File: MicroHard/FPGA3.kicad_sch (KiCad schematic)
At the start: 0 parts

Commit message: fpg
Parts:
- added U4: XC7A100T-FTG256, symbol FPGA_Xilinx_Artix7:XC7A100T-FTG256

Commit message: extra files
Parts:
- added C44: 47u, symbol Device:C
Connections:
- net +3.3V: now reaches U4.L6 (VCCO_0)
- net +3.3V: now also C44.1
- new net GND: C44.2
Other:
- moved on the sheet: U4C
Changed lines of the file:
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@@
 	(generator_version "8.0")
 	(paper "A4")
+	(wire
+		(pts
+			(xy 26.67 158.75) (xy 26.67 161.29)
+		)
+		(stroke
+			(width 0)
+			(type default)
+		)
+	)
+	(wire
+		(pts
+			(xy 26.67 168.91) (xy 26.67 170.18)
+		)
+		(stroke
+			(width 0)
+			(type default)
+		)
+	)
+	(wire
+		(pts
+			(xy 99.06 49.53) (xy 99.06 55.88)
+		)
+		(stroke
+			(width 0)
+			(type default)
+		)
+	)
+	(global_label "+3.3V"
+		(shape input)
+		(at 26.67 158.75 90)
+		(fields_autoplaced yes)
+		(effects
+			(font
+				(size 1.27 1.27)
+			)
+			(justify left)
+		)
+		(property "Intersheetrefs" "${INTERSHEET_REFS}"
+			(at 26.67 150.08 90)
+			(effects
+				(font
+					(size 1.27 1.27)
+				)
+				(justify left)
+				(hide yes)
+			)
+		)
+	)
+	(global_label "+3.3V"
+		(shape input)
+		(at 99.06 49.53 90)
+		(fields_autoplaced yes)
+		(effects
+			(font
+				(size 1.27 1.27)
+			)
+			(justify left)
+		)
+		(property "Intersheetrefs" "${INTERSHEET_REFS}"
+			(at 99.06 40.86 90)
+			(effects
+				(font
+					(size 1.27 1.27)
+				)
+				(justify left)
+				(hide yes)
+			)
+		)
+	)
+	(symbol
+		(lib_id "power:GND")
+		(at 26.67 170.18 0)
+		(unit 1)
+		(exclude_from_sim no)
+		(in_bom yes)
+		(on_board yes)
+		(dnp no)
+		(fields_autoplaced yes)
+		(property "Reference" "#PWR013"
+			(at 26.67 176.53 0)
+			(effects
+				(font
+					(size 1.27 1.27)
+				)
+				(hide yes)
+			)
+		)
+		(property "Value" "GND"
+			(at 26.67 175.26 0)
+			(effects
+				(font
+					(size 1.27 1.27)
+				)
+			)
+		)
+		(property "Footprint" ""
+			(at 26.67 170.18 0)
+			(effects
+				(font
+					(size 1.27 1.27)
+				)
+				(hide yes)
+			)
+		)
+		(property "Datasheet" ""
+			(at 26.67 170.18 0)
+			(effects
+				(font
+					(size 1.27 1.27)
+				)
+				(hide yes)
+			)
+		)
+		(property "Description" "Power symbol creates a global label with name \"GND\" , ground"
+			(at 26.67 170.18 0)
+			(effects
+				(font
+					(size 1.27 1.27)
+				)
+				(hide yes)
+			)
+		)
+		(pin "1"
+		)
+		(instances
+			(project ""
+				(path "/578bd531-a491-4b15-a479-460d159ffc14/e381883e-e672-4900-88a5-08b94f970a88/5897012d-c01f-459a-b65a-eba111a7dafb"
+					(reference "#PWR013")
+					(unit 1)
+				)
+			)
+		)
+	)
 	(symbol
 		(lib_id "FPGA_Xilinx_Artix7:XC7A100T-FTG256")
-		(at 90.17 88.9 0)
+		(at 71.12 96.52 0)
 		(unit 3)
 		(exclude_from_sim no)
@@
 		(fields_autoplaced yes)
 		(property "Reference" "U4"
-			(at 57.15 90.8049 0)
+			(at 38.1 98.4249 0)
 			(effects
 				(font
@@
 		)
 		(property "Value" "XC7A100T-FTG256"
-			(at 57.15 93.3449 0)
+			(at 38.1 100.9649 0)
 			(effects
 				(font
@@
 		)
 		(property "Footprint" ""
-			(at 90.17 88.9 0)
+			(at 71.12 96.52 0)
 			(effects
 				(font
@@
 		)
 		(property "Datasheet" ""
-			(at 90.17 88.9 0)
+			(at 71.12 96.52 0)
 			(effects
 				(font
@@
 		)
 		(property "Description" "Artix 7 T 100 XC7A100T-FTG256"
-			(at 90.17 88.9 0)
+			(at 71.12 96.52 0)
 			(effects
 				(font
@@
 				)
 			)
+		)
+	)
+	(symbol
+		(lib_id "Device:C")
+		(at 26.67 165.1 0)
+		(unit 1)
+		(exclude_from_sim no)
+		(in_bom yes)
+		(on_board yes)
+		(dnp no)
+		(fields_autoplaced yes)
+		(property "Reference" "C44"
+			(at 30.48 163.8299 0)
+			(effects
+				(font
+					(size 1.27 1.27)
+				)
+				(justify left)
+			)
+		)
+		(property "Value" "47u"
+			(at 30.48 166.3699 0)
+			(effects
+				(font
+					(size 1.27 1.27)
+				)
+				(justify left)
+			)
+		)
+		(property "Footprint" ""
+			(at 27.6352 168.91 0)
+			(effects
+				(font
+					(size 1.27 1.27)
+				)
+				(hide yes)
+			)
+		)
+		(property "Datasheet" "~"
+			(at 26.67 165.1 0)
+			(effects
+				(font
+					(size 1.27 1.27)
+				)
+				(hide yes)
+			)
+		)
+		(property "Description" "Unpolarized capacitor"
+			(at 26.67 165.1 0)
+			(effects
+				(font
+					(size 1.27 1.27)
+				)
+				(hide yes)
+			)
+		)
+		(pin "1"
+		)
+		(pin "2"
+		)
+		(instances
+			(project ""
+				(path "/578bd531-a491-4b15-a479-460d159ffc14/e381883e-e672-4900-88a5-08b94f970a88/5897012d-c01f-459a-b65a-eba111a7dafb"
+					(reference "C44")
+					(unit 1)
+				)
+			)

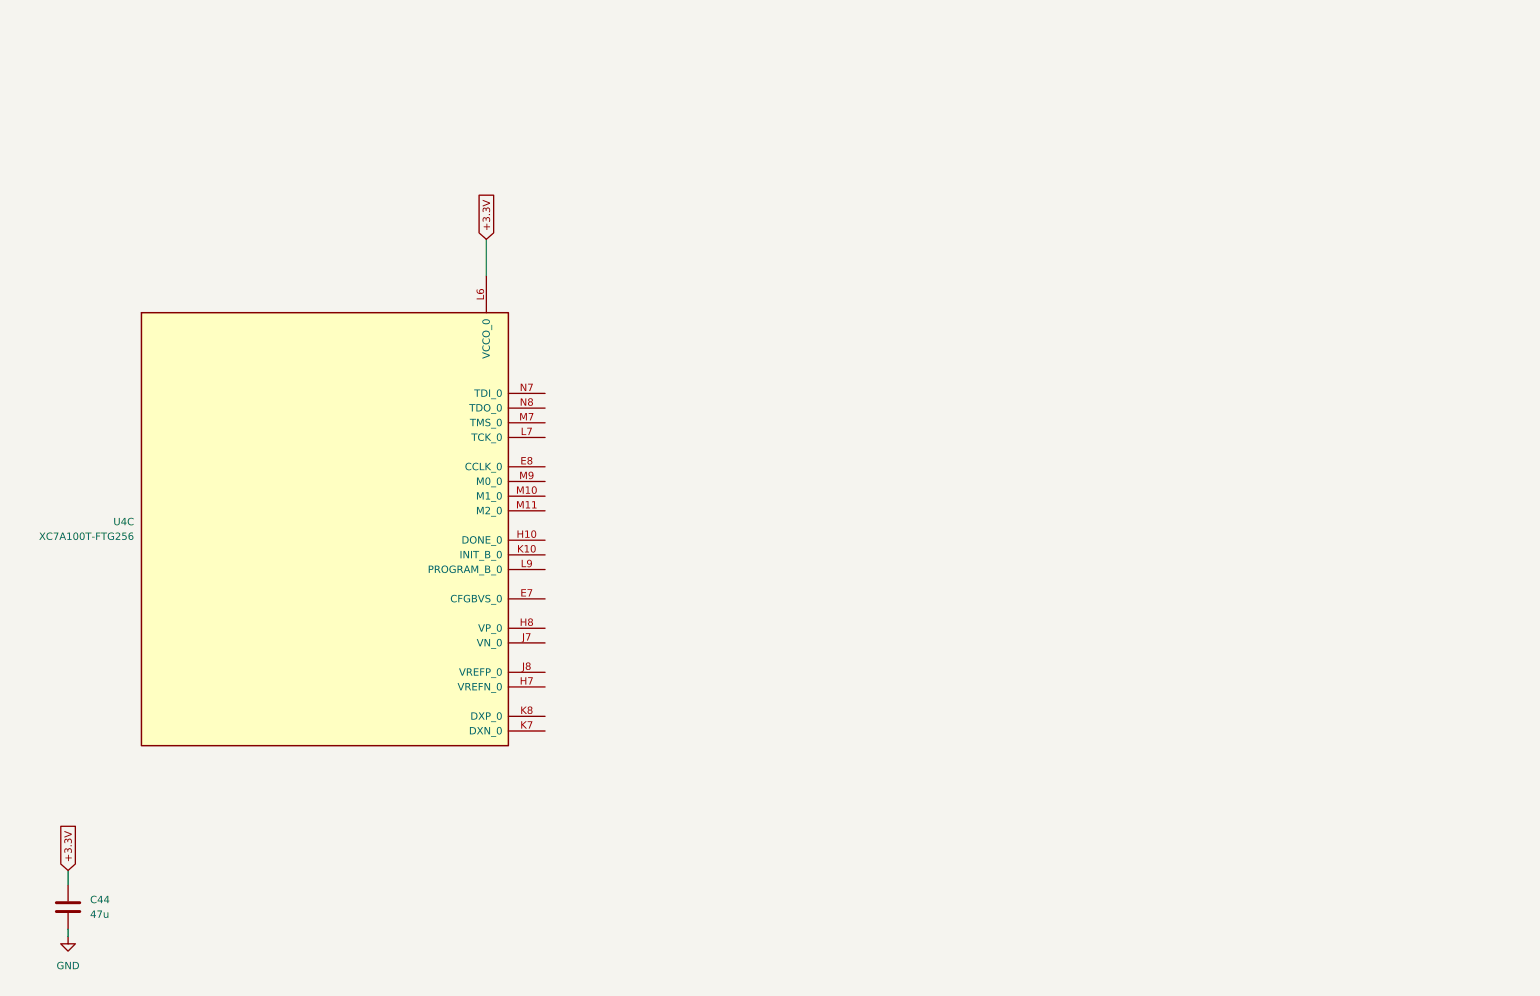
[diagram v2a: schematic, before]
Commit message: feat: finished FPGA config
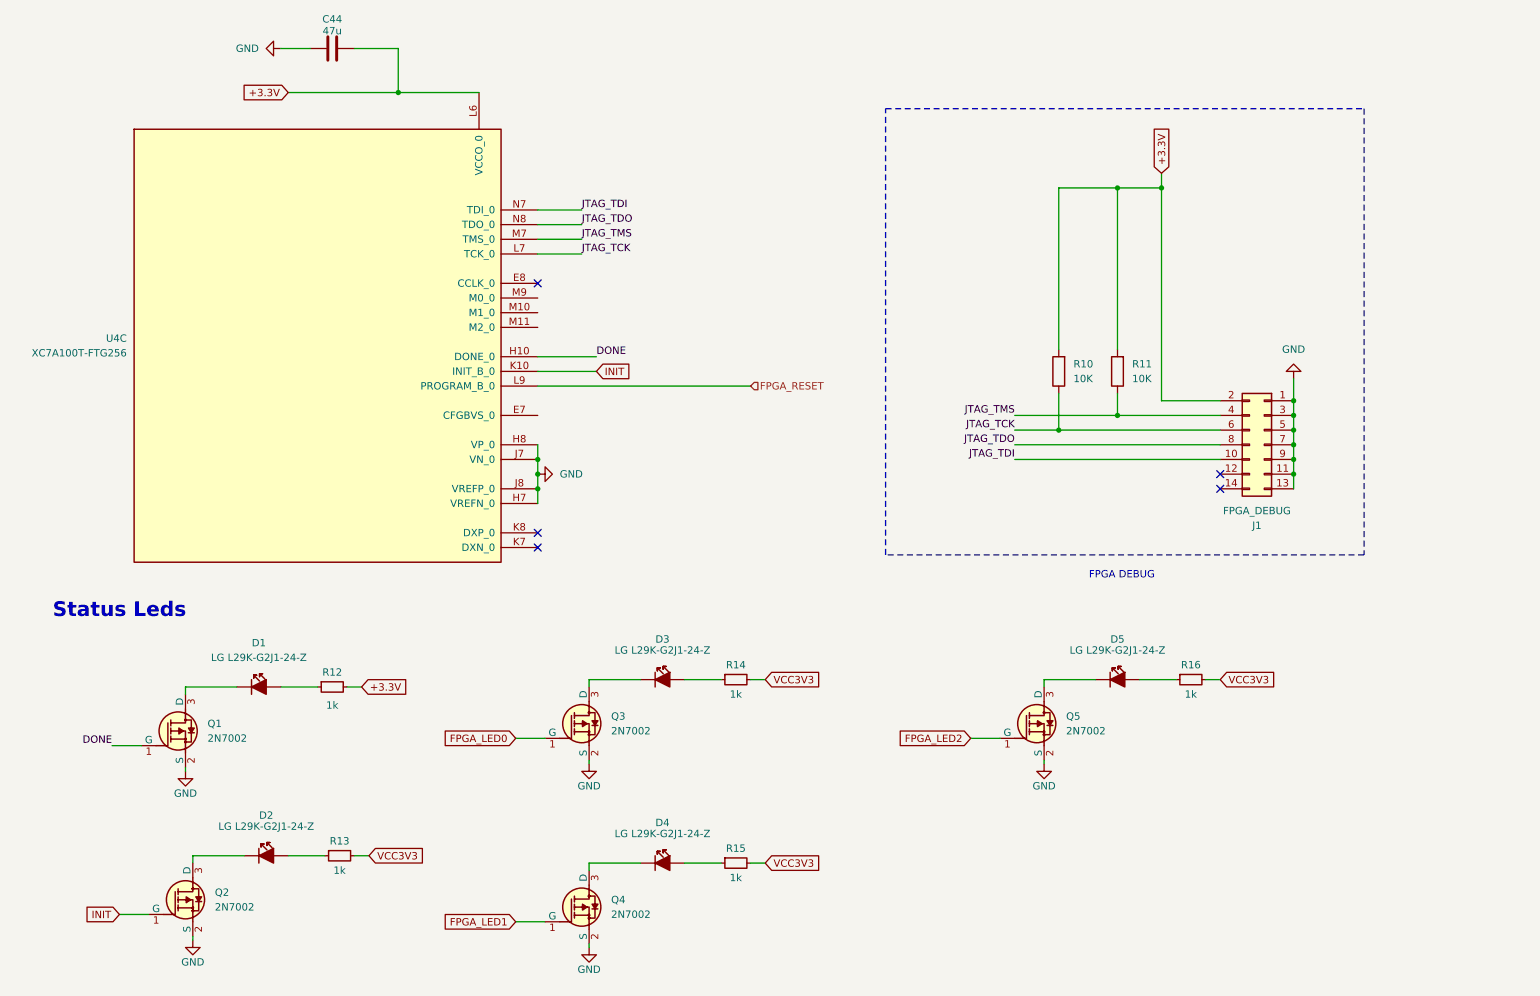
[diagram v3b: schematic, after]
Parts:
- added D1, D2, D3, D4, D5: LED_G_0603_LG_L29K-G2J1-24-Z, antmicro-footprints:LED_0603_1608Metric_G, symbol antmicroLEDIndicationDiscrete:LED_G_0603_LG_L29K-G2J1-24-Z
- added J1: FPGA_DEBUG, symbol Connector_Generic:Conn_02x07_Odd_Even
- added Q1, Q2, Q3, Q4, Q5: 2N7002_SOT-23-3, antmicro-footprints:SOT-23-3, symbol antmicroTransistorsFETsMOSFETsSingle:2N7002_SOT-23-3
- added R10, R11: 10K, symbol Device:R
- added R12, R13, R14, R15, R16: R_1k_0402, antmicro-footprints:R_0402_1005Metric, symbol antmicroResistors0402:R_1k_0402
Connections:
- net +3.3V: now also J1.2 (Pin_2), R10.2, R11.2, R12.2
- net GND: now also U4.H7 (VREFN_0), U4.H8 (VP_0), U4.J7 (VN_0), U4.J8 (VREFP_0), J1.1 (Pin_1), J1.11 (Pin_11), J1.13 (Pin_13), J1.3 (Pin_3), J1.5 (Pin_5), J1.7 (Pin_7), J1.9 (Pin_9), Q1.2 (S), Q2.2 (S), Q3.2 (S), Q4.2 (S), Q5.2 (S)
- net DONE: now reaches U4.H10 (DONE_0)
- net DONE: now also Q1.1 (G)
- net INIT: now reaches U4.K10 (INIT_B_0)
- net INIT: now also Q2.1 (G)
- net JTAG_TCK: now reaches U4.L7 (TCK_0)
- net JTAG_TCK: now also J1.6 (Pin_6), R10.1
- net FPGA_RESET: now reaches U4.L9 (PROGRAM_B_0)
- net JTAG_TMS: now reaches U4.M7 (TMS_0)
- net JTAG_TMS: now also J1.4 (Pin_4), R11.1
- net JTAG_TDI: now reaches U4.N7 (TDI_0)
- net JTAG_TDI: now also J1.10 (Pin_10)
- net JTAG_TDO: now reaches U4.N8 (TDO_0)
- net JTAG_TDO: now also J1.8 (Pin_8)
- new net: D1.1, R12.1
- new net: D5.1, R16.1
- new net: D5.2, Q5.3 (D)
- new net: D3.2, Q3.3 (D)
- new net: D3.1, R14.1
- new net: D2.1, R13.1
- new net: D1.2, Q1.3 (D)
- new net: D4.1, R15.1
- new net: D4.2, Q4.3 (D)
- new net: D2.2, Q2.3 (D)
- new net FPGA_LED0: Q3.1 (G)
- new net FPGA_LED1: Q4.1 (G)
- new net FPGA_LED2: Q5.1 (G)
- new net VCC3V3: R13.2, R14.2, R15.2, R16.2
- no-connect marks 0 -> 5
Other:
- note added: "FPGA DEBUG"
- note added: "Status Leds"
- moved on the sheet: U4C

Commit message: feat: finished Flash mem and FPGA Config
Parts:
- added R17, R19: 4.7k, symbol Device:R
- added R18: 330, symbol Device:R
- added TP1, TP2, TP3: TestPoint, symbol Connector:TestPoint
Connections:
- net +3.3V: now also U4.E7 (CFGBVS_0), U4.M9 (M0_0), R17.1, R18.2, R19.1
- net FPGA_RESET: now also Q1.1 (G), R19.2, TP1.1, TP2.1
- net GND: now also U4.M10 (M1_0), U4.M11 (M2_0)
- net INIT: now also R17.2, TP3.1
- net FPGA_CONFIG_CLOCK: now reaches U4.E8 (CCLK_0)
- net DONE: no longer names the net of U4.H10 (DONE_0)
- net DONE: now also R18.1; no longer Q1.1 (G)
- no-connect marks 5 -> 4
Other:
- note added: "Are these pull ups neccessary"
- moved on the sheet: J1, R10, R11

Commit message: chore
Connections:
- net VCC3V3 is gone; now on net +3.3V: R13.2, R14.2, R15.2, R16.2
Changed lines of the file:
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@@
+		)
+	)
+	(global_label "+3.3V"
+		(shape input)
+		(at 147.32 125.73 0)
+		(fields_autoplaced yes)
+		(effects
+			(font
+				(size 1.27 1.27)
+			)
+			(justify left)
+		)
+		(property "Intersheetrefs" "${INTERSHEET_REFS}"
+			(at 155.99 125.73 0)
+			(effects
+				(font
+					(size 1.27 1.27)
+				)
+				(justify left)
+				(hide yes)
+			)
 		)
 	)
@@
 		)
 	)
-	(global_label "VCC3V3"
+	(global_label "+3.3V"
+		(shape input)
+		(at 78.74 156.21 0)
+		(fields_autoplaced yes)
+		(effects
+			(font
+				(size 1.27 1.27)
+			)
+			(justify left)
+		)
+		(property "Intersheetrefs" "${INTERSHEET_REFS}"
+			(at 87.41 156.21 0)
+			(effects
+				(font
+					(size 1.27 1.27)
+				)
+				(justify left)
+				(hide yes)
+			)
+		)
+	)
+	(global_label "FPGA_LED1"
+		(shape input)
+		(at 104.14 167.64 180)
+		(fields_autoplaced yes)
+		(effects
+			(font
+				(size 1.27 1.27)
+			)
+			(justify right)
+		)
+		(property "Intersheetrefs" "${INTERSHEET_REFS}"
+			(at 90.8134 167.64 0)
+			(effects
+				(font
+					(size 1.27 1.27)
+				)
+				(justify right)
+				(hide yes)
+			)
+		)
+	)
+	(global_label "FPGA_LED2"
+		(shape input)
+		(at 182.88 135.89 180)
+		(fields_autoplaced yes)
+		(effects
+			(font
+				(size 1.27 1.27)
+			)
+			(justify right)
+		)
+		(property "Intersheetrefs" "${INTERSHEET_REFS}"
+			(at 169.5534 135.89 0)
+			(effects
+				(font
+					(size 1.27 1.27)
+				)
+				(justify right)
+				(hide yes)
+			)
+		)
+	)
+	(global_label "+3.3V"
+		(shape input)
+		(at 77.47 127 0)
+		(fields_autoplaced yes)
+		(effects
+			(font
+				(size 1.27 1.27)
+			)
+			(justify left)
+		)
+		(property "Intersheetrefs" "${INTERSHEET_REFS}"
+			(at 86.14 127 0)
+			(effects
+				(font
+					(size 1.27 1.27)
+				)
+				(justify left)
+				(hide yes)
+			)
+		)
+	)
+	(global_label "+3.3V"
+		(shape input)
+		(at 147.32 157.48 0)
+		(fields_autoplaced yes)
+		(effects
+			(font
+				(size 1.27 1.27)
+			)
+			(justify left)
+		)
+		(property "Intersheetrefs" "${INTERSHEET_REFS}"
+			(at 155.99 157.48 0)
+			(effects
+				(font
+					(size 1.27 1.27)
+				)
+				(justify left)
+				(hide yes)
+			)
+		)
+	)
+	(global_label "+3.3V"
 		(shape input)
 		(at 226.06 125.73 0)
@@
 		)
 		(property "Intersheetrefs" "${INTERSHEET_REFS}"
-			(at -59.055 96.52 0)
-			(effects
-				(font
-					(size 1.27 1.27)
-				)
-				(hide yes)
-			)
-		)
-	)
-	(global_label "FPGA_LED1"
-		(shape input)
-		(at 104.14 167.64 180)
-		(fields_autoplaced yes)
-		(effects
-			(font
-				(size 1.27 1.27)
-			)
-			(justify right)
-		)
-		(property "Intersheetrefs" "${INTERSHEET_REFS}"
-			(at 90.8134 167.64 0)
-			(effects
-				(font
-					(size 1.27 1.27)
-				)
-				(justify right)
-				(hide yes)
-			)
-		)
-	)
-	(global_label "FPGA_LED2"
-		(shape input)
-		(at 182.88 135.89 180)
-		(fields_autoplaced yes)
-		(effects
-			(font
-				(size 1.27 1.27)
-			)
-			(justify right)
-		)
-		(property "Intersheetrefs" "${INTERSHEET_REFS}"
-			(at 169.5534 135.89 0)
-			(effects
-				(font
-					(size 1.27 1.27)
-				)
-				(justify right)
-				(hide yes)
-			)
-		)
-	)
-	(global_label "+3.3V"
-		(shape input)
-		(at 77.47 127 0)
-		(fields_autoplaced yes)
-		(effects
-			(font
-				(size 1.27 1.27)
-			)
-			(justify left)
-		)
-		(property "Intersheetrefs" "${INTERSHEET_REFS}"
-			(at 86.14 127 0)
+			(at 234.73 125.73 0)
 			(effects
 				(font
@@
 		)
 	)
-	(global_label "VCC3V3"
-		(shape input)
-		(at 147.32 157.48 0)
-		(fields_autoplaced yes)
-		(effects
-			(font
-				(size 1.27 1.27)
-			)
-			(justify left)
-		)
-		(property "Intersheetrefs" "${INTERSHEET_REFS}"
-			(at -137.795 128.27 0)
-			(effects
-				(font
-					(size 1.27 1.27)
-				)
-				(hide yes)
-			)
-		)
-	)
 	(global_label "INIT"
 		(shape input)
@@
 				(hide yes)
 			)
-		)
-	)
-	(global_label "VCC3V3"
-		(shape input)
-		(at 147.32 125.73 0)
-		(fields_autoplaced yes)
-		(effects
-			(font
-				(size 1.27 1.27)
-			)
-			(justify left)
-		)
-		(property "Intersheetrefs" "${INTERSHEET_REFS}"
-			(at -137.795 96.52 0)
-			(effects
-				(font
-					(size 1.27 1.27)
-				)
-				(hide yes)
-			)
-		)
-	)
-	(global_label "VCC3V3"
-		(shape input)
-		(at 78.74 156.21 0)
-		(fields_autoplaced yes)
-		(effects
-			(font
-				(size 1.27 1.27)
-			)
-			(justify left)
-		)
-		(property "Intersheetrefs" "${INTERSHEET_REFS}"
-			(at -206.375 127 0)
-			(effects
-				(font
-					(size 1.27 1.27)
-				)
-				(hide yes)
-			)
